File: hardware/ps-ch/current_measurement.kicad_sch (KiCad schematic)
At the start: 3 parts, among them U6 INA301A3

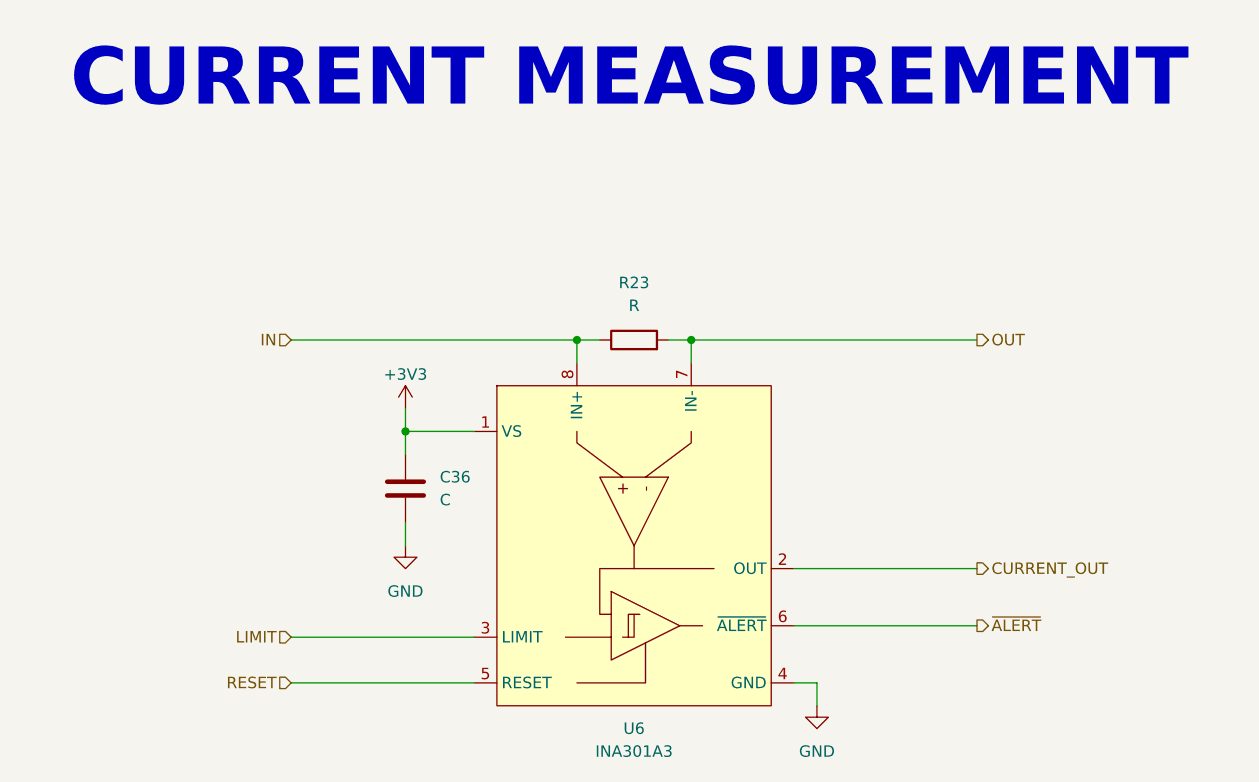
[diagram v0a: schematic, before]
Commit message: - added component values/part numbers
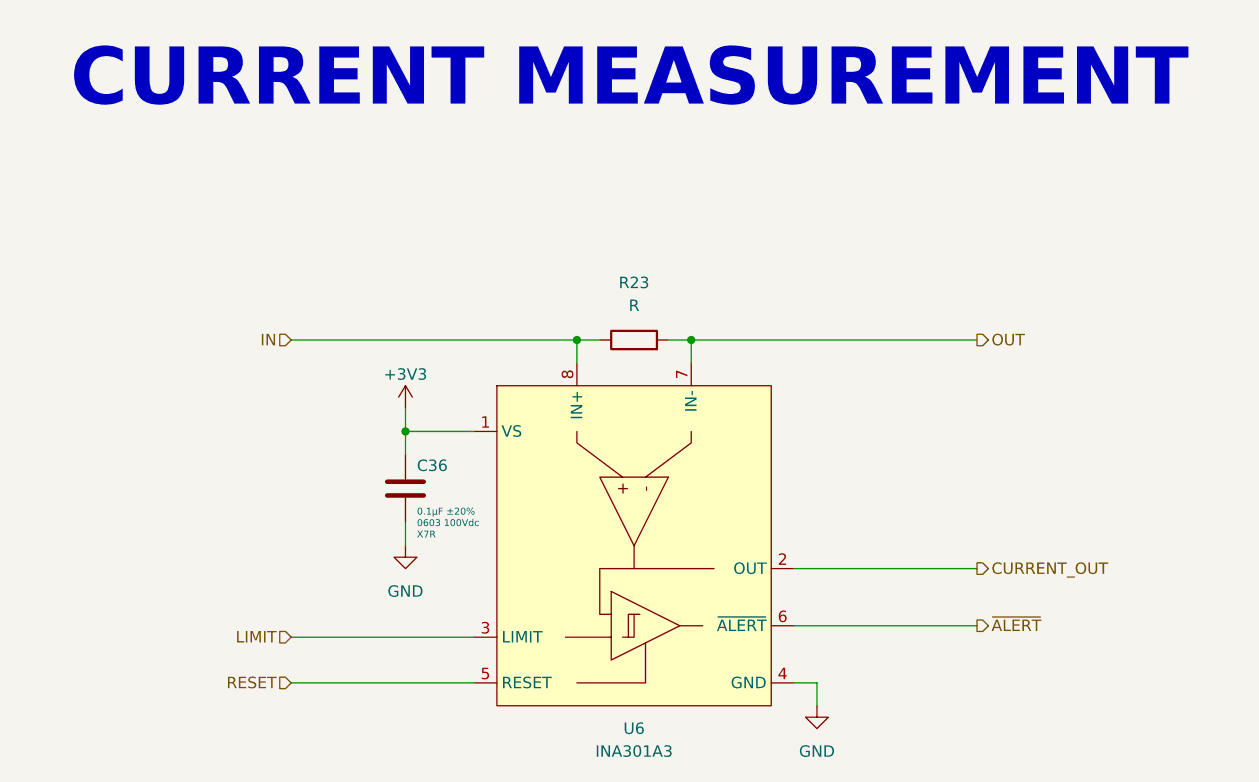
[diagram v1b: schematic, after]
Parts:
- C36: value C -> 0.1μF 0603 100Vdc X7R ±20%; footprint (none) -> Capacitor_SMD:C_0603_1608Metric; symbol Device:C -> ps-ch:0.1μF 0603 100Vdc X7R ±20%; DisplayValue0 (none) -> 0.1μF ±20%; DisplayValue1 (none) -> 0603 100Vdc; DisplayValue2 (none) -> X7R; Manufacturer (none) -> Murata; Manufacturer Part Number (none) -> GRM188R72A104MA35
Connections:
- net +3V3: now also C36.2; no longer C36.1
- net GND: now also C36.1; no longer C36.2
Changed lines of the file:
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@@
 	)
 	(symbol
-		(lib_id "Device:C")
+		(lib_id "ps-ch:0.1μF 0603 100Vdc X7R ±20%")
 		(at 119.38 87.63 0)
 		(unit 1)
@@
 		(on_board yes)
 		(dnp no)
-		(fields_autoplaced yes)
 		(property "Reference" "C36"
-			(at 123.19 86.3599 0)
+			(at 120.65 85.09 0)
 			(effects
 				(font
@@
 			)
 		)
-		(property "Value" "C"
-			(at 123.19 88.8999 0)
+		(property "Value" "0.1μF 0603 100Vdc X7R ±20%"
+			(at 119.38 72.39 0)
 			(effects
 				(font
 					(size 1.27 1.27)
 				)
-				(justify left)
+				(hide yes)
 			)
 		)
-		(property "Footprint" ""
-			(at 120.3452 91.44 0)
+		(property "Footprint" "Capacitor_SMD:C_0603_1608Metric"
+			(at 119.38 77.47 0)
 			(effects
 				(font
@@
 		)
 		(property "Datasheet" "~"
-			(at 119.38 87.63 0)
+			(at 119.38 87.63 90)
+			(effects
+				(font
+					(size 1 1)
+				)
+				(hide yes)
+			)
+		)
+		(property "Description" "Capacitor 0603 100Vdc X7R ±20%"
+			(at 119.38 74.93 0)
 			(effects
 				(font
@@
 			)
 		)
-		(property "Description" "Unpolarized capacitor"
-			(at 119.38 87.63 0)
+		(property "Manufacturer" "Murata"
+			(at 119.38 67.31 0)
 			(effects
 				(font
@@
 			)
 		)
+		(property "Manufacturer Part Number" "GRM188R72A104MA35"
+			(at 119.38 69.85 0)
+			(effects
+				(font
+					(size 1.27 1.27)
+				)
+				(hide yes)
+			)
+		)
+		(property "DisplayValue0" "0.1μF ±20%"
+			(at 120.65 90.17 0)
+			(effects
+				(font
+					(size 0.762 0.762)
+				)
+				(justify left)
+			)
+		)
+		(property "DisplayValue1" "0603 100Vdc"
+			(at 120.65 91.44 0)
+			(effects
+				(font
+					(size 0.762 0.762)
+				)
+				(justify left)
+			)
+		)
+		(property "DisplayValue2" "X7R"
+			(at 120.65 92.71 0)
+			(effects
+				(font
+					(size 0.762 0.762)
+				)
+				(justify left)
+			)
+		)

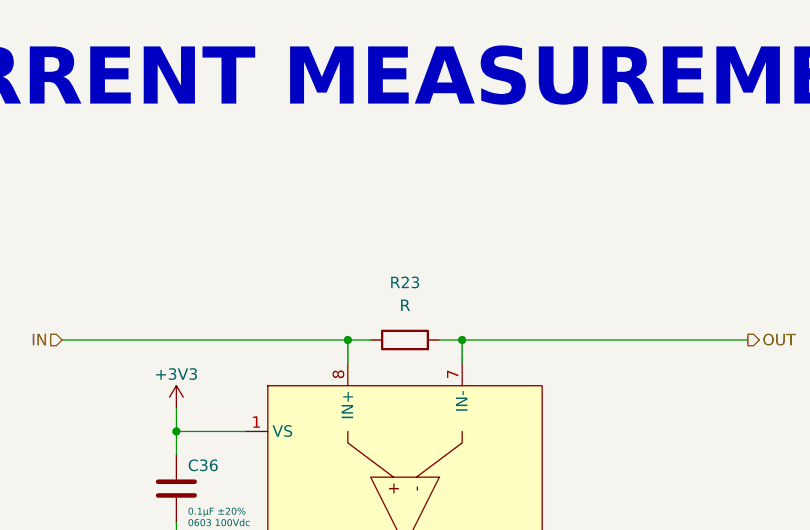
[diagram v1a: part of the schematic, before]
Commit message: wired adc/added resolutions
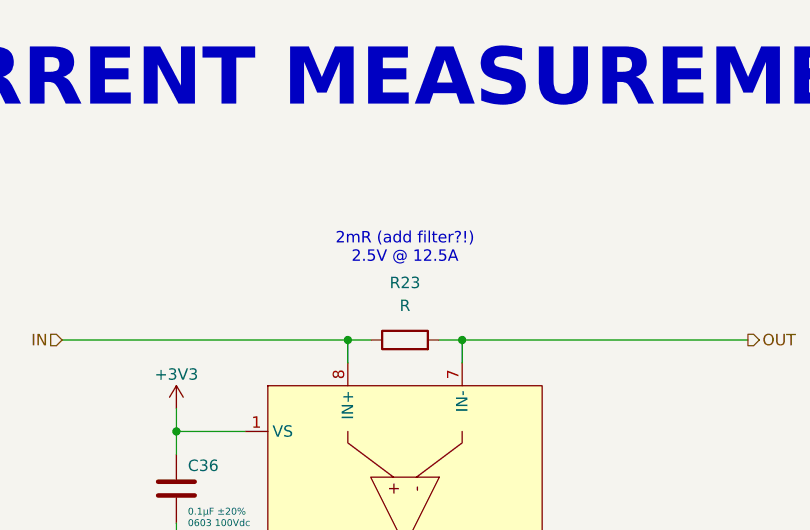
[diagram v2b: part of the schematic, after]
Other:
- note added: "2mR (add filter?!) 2.5V @ 12.5A"
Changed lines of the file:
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@@
 	(generator_version "9.0")
 	(paper "A4")
+	(text "2mR (add filter?!)\n2.5V @ 12.5A"
+		(exclude_from_sim no)
+		(at 144.78 60.96 0)
+		(effects
+			(font
+				(size 1.27 1.27)
+			)
+		)
+	)
 	(text "CURRENT MEASUREMENT"
 		(exclude_from_sim no)

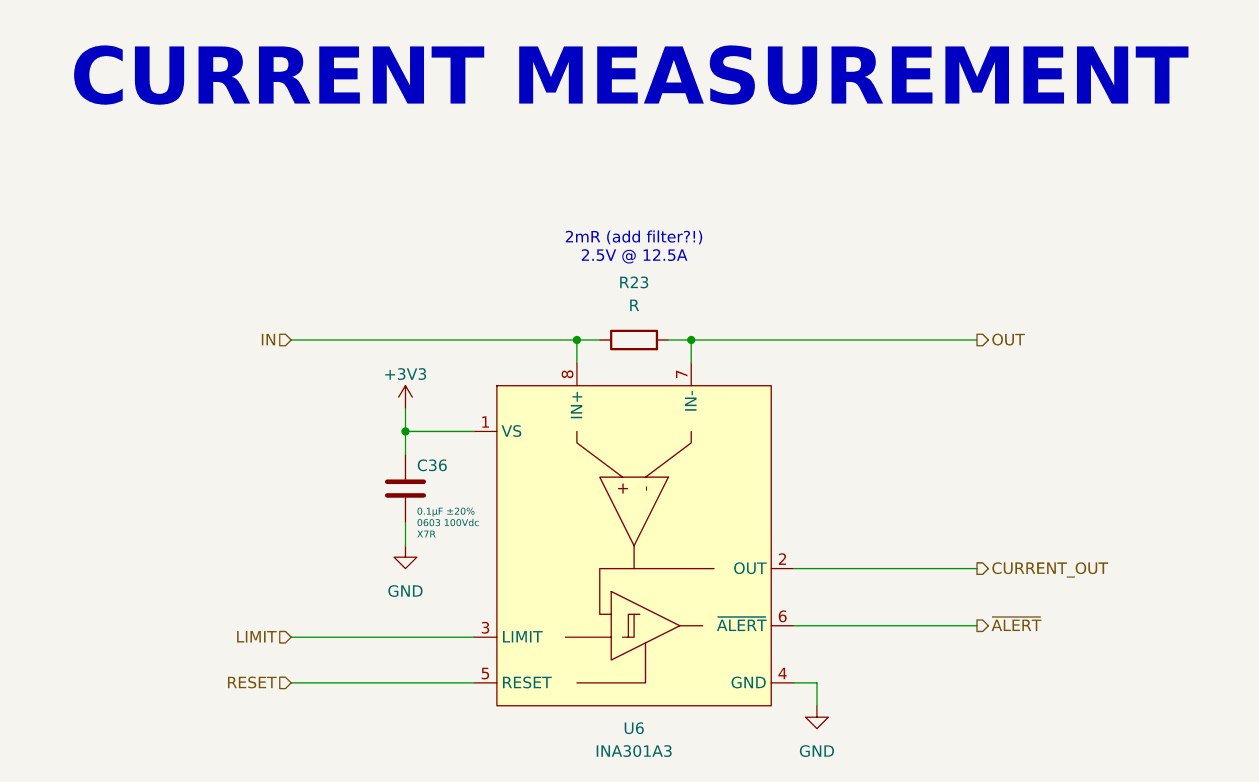
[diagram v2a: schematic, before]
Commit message: parameterized flyback converter
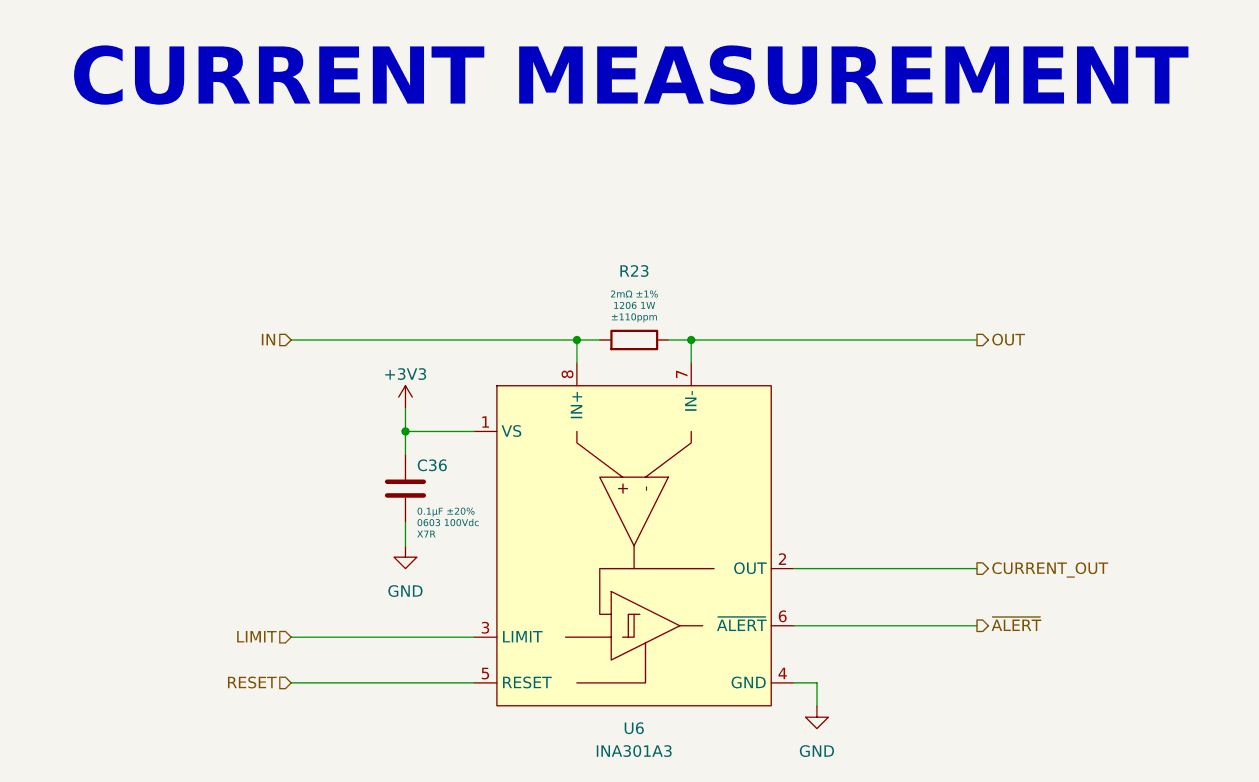
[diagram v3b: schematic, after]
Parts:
- R23: value R -> 2mΩ 1206 1W ±1% ±50ppm/°C; footprint (none) -> Resistor_SMD:R_1206_3216Metric; symbol Device:R -> ps-ch:2mΩ 1206 1W ±1% ±50ppm/°C; DisplayValue0 (none) -> 2mΩ ±1%; DisplayValue1 (none) -> 1206 1W; DisplayValue2 (none) -> ±110ppm; Manufacturer (none) -> Bourns; Manufacturer Part Number (none) -> CRF1206FZR002ELF
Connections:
- net IN: now also R23.2; no longer R23.1
- net OUT: now also R23.1; no longer R23.2
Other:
- note removed: "2mR (add filter?!) 2.5V @ 12.5A"
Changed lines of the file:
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@@
 	(generator_version "9.0")
 	(paper "A4")
-	(text "2mR (add filter?!)\n2.5V @ 12.5A"
-		(exclude_from_sim no)
-		(at 144.78 60.96 0)
-		(effects
-			(font
-				(size 1.27 1.27)
-			)
-		)
-	)
 	(text "CURRENT MEASUREMENT"
 		(exclude_from_sim no)
@@
 	)
 	(symbol
-		(lib_id "Device:R")
+		(lib_id "ps-ch:2mΩ 1206 1W ±1% ±50ppm/°C")
 		(at 144.78 71.12 90)
 		(unit 1)
@@
 		(fields_autoplaced yes)
 		(property "Reference" "R23"
-			(at 144.78 64.77 90)
+			(at 144.8054 63.5 90)
 			(effects
 				(font
@@
 			)
 		)
-		(property "Value" "R"
-			(at 144.78 67.31 90)
+		(property "Value" "2mΩ 1206 1W ±1% ±50ppm/°C"
+			(at 129.54 71.12 0)
 			(effects
 				(font
 					(size 1.27 1.27)
 				)
-			)
-		)
-		(property "Footprint" ""
-			(at 144.78 72.898 90)
+				(hide yes)
+			)
+		)
+		(property "Footprint" "Resistor_SMD:R_1206_3216Metric"
+			(at 134.62 71.12 0)
 			(effects
 				(font
@@
 		)
 		(property "Datasheet" "~"
-			(at 144.78 71.12 0)
+			(at 144.78 71.12 90)
+			(effects
+				(font
+					(size 1 1)
+				)
+				(hide yes)
+			)
+		)
+		(property "Description" "R 1206 1W ±1% ±50ppm/°C"
+			(at 132.08 71.12 0)
 			(effects
 				(font
@@
 			)
 		)
-		(property "Description" "Resistor"
-			(at 144.78 71.12 0)
+		(property "Manufacturer" "Bourns"
+			(at 124.46 71.12 0)
 			(effects
 				(font
@@
 			)
 		)
+		(property "Manufacturer Part Number" "CRF1206FZR002ELF"
+			(at 127 71.12 0)
+			(effects
+				(font
+					(size 1.27 1.27)
+				)
+				(hide yes)
+			)
+		)
+		(property "DisplayValue0" "2mΩ ±1%"
+			(at 144.8054 66.04 90)
+			(effects
+				(font
+					(size 0.762 0.762)
+				)
+			)
+		)
+		(property "DisplayValue1" "1206 1W"
+			(at 144.8054 67.31 90)
+			(effects
+				(font
+					(size 0.762 0.762)
+				)
+			)
+		)
+		(property "DisplayValue2" "±110ppm"
+			(at 144.8054 68.58 90)
+			(effects
+				(font
+					(size 0.762 0.762)
+				)
+			)
+		)

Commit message: assigned footprints
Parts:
- U6: footprint (none) -> Package_SO:VSSOP-8_3x3mm_P0.65mm; Manufacturer (none) -> Texas Instruments; Manufacturer Part Number (none) -> INA301A3IDGKR
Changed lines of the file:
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@@
 			)
 		)
-		(property "Footprint" ""
+		(property "Footprint" "Package_SO:VSSOP-8_3x3mm_P0.65mm"
 			(at 144.78 93.98 0)
 			(effects
@@
 			)
 		)
-		(property "Datasheet" ""
+		(property "Datasheet" "https://www.ti.com/lit/ds/symlink/ina301.pdf?ts=1758771169210&ref_url=https%253A%252F%252Fwww.ti.com%252Fproduct%252FINA301"
 			(at 144.78 93.98 0)
 			(effects
@@
 			(effects
 				(font
+					(size 1.27 1.27)
+				)
+				(hide yes)
+			)
+		)
+		(property "Manufacturer" "Texas Instruments"
+			(at 144.78 55.88 0)
+			(effects
+				(font
+					(size 1.27 1.27)
+				)
+				(hide yes)
+			)
+		)
+		(property "Manufacturer Part Number" "INA301A3IDGKR"
+			(at 144.78 58.42 0)
+			(effects
+				(font

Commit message: first pcb sync
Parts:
- renumbered C36 to C89, R23 to R81, U6 to U18
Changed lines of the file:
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@@
 		(dnp no)
 		(fields_autoplaced yes)
-		(property "Reference" "R23"
+		(property "Reference" "R81"
 			(at 144.8054 63.5 90)
 			(effects
@@
 			(project "ps-ch"
 				(path "/431acd2e-2ab9-4aa9-b759-273f044decc5/d894c1fd-b786-4989-9577-d72811ca5dd8"
-					(reference "R23")
+					(reference "R81")
 					(unit 1)
 				)
@@
 		(on_board yes)
 		(dnp no)
-		(property "Reference" "#PWR053"
+		(property "Reference" "#PWR0167"
 			(at 119.38 82.55 0)
 			(effects
@@
 			(project "ps-ch"
 				(path "/431acd2e-2ab9-4aa9-b759-273f044decc5/d894c1fd-b786-4989-9577-d72811ca5dd8"
-					(reference "#PWR053")
+					(reference "#PWR0167")
 					(unit 1)
 				)
@@
 		(dnp no)
 		(fields_autoplaced yes)
-		(property "Reference" "#PWR052"
+		(property "Reference" "#PWR0168"
 			(at 119.38 100.33 0)
 			(effects
@@
 			(project "ps-ch"
 				(path "/431acd2e-2ab9-4aa9-b759-273f044decc5/d894c1fd-b786-4989-9577-d72811ca5dd8"
-					(reference "#PWR052")
+					(reference "#PWR0168")
 					(unit 1)
 				)
@@
 		(on_board yes)
 		(dnp no)
-		(property "Reference" "C36"
+		(property "Reference" "C89"
 			(at 120.65 85.09 0)
 			(effects
@@
 			(project "ps-ch"
 				(path "/431acd2e-2ab9-4aa9-b759-273f044decc5/d894c1fd-b786-4989-9577-d72811ca5dd8"
-					(reference "C36")
+					(reference "C89")
 					(unit 1)
 				)
@@
 		(dnp no)
 		(fields_autoplaced yes)
-		(property "Reference" "#PWR051"
+		(property "Reference" "#PWR0169"
 			(at 165.1 118.11 0)
 			(effects
@@
 			(project "ps-ch"
 				(path "/431acd2e-2ab9-4aa9-b759-273f044decc5/d894c1fd-b786-4989-9577-d72811ca5dd8"
-					(reference "#PWR051")
+					(reference "#PWR0169")
 					(unit 1)
 				)
@@
 		(dnp no)
 		(fields_autoplaced yes)
-		(property "Reference" "U6"
+		(property "Reference" "U18"
 			(at 144.78 114.3 0)
 			(effects
@@
 			(project "ps-ch"
 				(path "/431acd2e-2ab9-4aa9-b759-273f044decc5/d894c1fd-b786-4989-9577-d72811ca5dd8"
-					(reference "U6")
-					(unit 1)
-				)
+					(reference "U18")
+					(unit 1)
+				)
